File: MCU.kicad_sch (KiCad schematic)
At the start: 36 parts

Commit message: Updates to schematic
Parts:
- removed C?: 100n, Capacitor_SMD:C_0603_1608Metric_Pad1.08x0.95mm_HandSolder, symbol Device:C_Small
- removed D? (x4): BAT54S, Package_TO_SOT_SMD:SOT-23, symbol Diode:BAT54S
- removed J?: LED_MCU_ON, symbol Connector_Generic:Conn_01x02
- removed J?: DNP, Connector_Coaxial:U.FL_Molex_MCRF_73412-0110_Vertical, symbol Connector:Conn_Coaxial
- removed R?: 470, Resistor_SMD:R_0603_1608Metric_Pad0.98x0.95mm_HandSolder, symbol Device:R
- removed R? (x2): 10k, Resistor_SMD:R_0603_1608Metric_Pad0.98x0.95mm_HandSolder, symbol Device:R
- removed U?: 74LVC1G66, Package_TO_SOT_SMD:SOT-353_SC-70-5_Handsoldering, symbol 74xGxx:74LVC1G66
- added C? (x5): 100n, Capacitor_SMD:C_0603_1608Metric_Pad1.08x0.95mm_HandSolder, symbol Device:C_Small
- added D?: PLL_LOCK, LED_SMD:LED_0603_1608Metric_Pad1.05x0.95mm_HandSolder, symbol Device:LED
- added D? (x8): (no value), LED_SMD:LED_0603_1608Metric_Pad1.05x0.95mm_HandSolder, symbol Device:LED
- added D? (x12): PESD3V3L4UG, Package_TO_SOT_SMD:SOT-353_SC-70-5, symbol Power_Protection:PESD3V3L4UG
- added FB?: TODO, symbol Device:FerriteBead_Small
- added J? (x2): Conn_01x03, symbol Connector_Generic:Conn_01x03
- added J?: Conn_01x06, symbol Connector_Generic:Conn_01x06
- added R? (x4): 100, Resistor_SMD:R_0603_1608Metric_Pad0.98x0.95mm_HandSolder, symbol Device:R
- added R? (x9): 2k, Resistor_SMD:R_0603_1608Metric_Pad0.98x0.95mm_HandSolder, symbol Device:R
- added R? (x5): 10k, Resistor_SMD:R_0603_1608Metric_Pad0.98x0.95mm_HandSolder, symbol Device:R
- added R?: 3k3, Resistor_SMD:R_0603_1608Metric_Pad0.98x0.95mm_HandSolder, symbol Device:R
- added R?: NC, Resistor_SMD:R_0603_1608Metric_Pad0.98x0.95mm_HandSolder, symbol Device:R
- added U? (x2): 74HC4094, Package_SO:SO-16_3.9x9.9mm_P1.27mm, symbol petr:74HC4094
- added U?: SN75176AD, Package_SO:SOIC-8_3.9x4.9mm_P1.27mm, symbol Interface_UART:SN75176AD
- added Y?: Crystal_GND24, symbol Device:Crystal_GND24
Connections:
- net AVDD: now also FB?.2
- net CE: now also U?.12 (Q6)
- net CLK_SEL: now also R?.2, U?.7 (Q3)
- net CSB: now also U?.28 (PA07)
- net DIVA: now also U?.40 (PD00)
- net DIVB: now also U?.39 (PD01)
- net GND: now also C?.2, C?.2, C?.2, C?.2, C?.2, D?.2 (A), D?.2 (A), D?.2 (A), J?.3 (Pin_3), J?.3 (Pin_3), J?.6 (Pin_6), R?.1, R?.1, R?.1, R?.1, R?.2, R?.2, R?.2, R?.2, R?.2, R?.2, R?.2, R?.2, R?.2, R?.2, U?.5 (GND), U?.8 (GND), U?.8 (GND), Y?.2, Y?.4
- net LOS_0: now also U?.17 (PB03)
- net LOS_1: now also U?.16 (PB04)
- net MUXout: now also U?.27 (PA06)
- net OE_B: now also R?.2, U?.13 (Q5)
- net PLL_ON: now also U?.4 (Q0)
- net RampClk: now also U?.29 (PA08)
- net RampDir: now also U?.11 (Q7)
- net SCK: now also U?.25 (PA04)
- net SDI: now also U?.26 (PA05)
- net SFOUTB_0: now also U?.38 (PD02)
- net SFOUTB_1: now also U?.37 (PD03)
- net SWCLK: now also D?.5 (K4)
- net SWDIO: now also D?.4 (K3)
- net SWO: now also D?.3 (K2)
- net TCXO_ON: now also U?.6 (Q2)
- net VCC_TCXO: now also U?.21 (PA00)
- net fREF_ON: now also U?.5 (Q1)
- net ~{DF_CORR_EN}: now also U?.14 (Q4)
- net AUX_CLK: now reaches U?.1 (PC00)
- net AUX_CLK: now also R?.1, U?.3 (CP), U?.3 (CP)
- net at U?.10 (HFXTAL_O): now also Y?.3
- net ~{RESET}: now reaches U?.11 (RESETN)
- net ~{RESET}: now also C?.1, D?.1 (K1), R?.1
- net RS485_DIR: now reaches U?.18 (PB02)
- net RS485_DIR: now also R?.1, U?.2 (~{RE}), U?.3 (DE)
- net RS485_TX: now reaches U?.19 (PB01)
- net RS485_TX: now also U?.4 (D)
- net AUX_D: now reaches U?.2 (PC01)
- net AUX_D: now also U?.2 (D)
- net RS485_RX: now reaches U?.20 (PB00)
- net RS485_RX: now also U?.1 (R)
- net AUX_STR: now reaches U?.3 (PC02)
- net AUX_STR: now also R?.1, U?.1 (STR), U?.1 (STR)
- net AUX_OE: now reaches U?.4 (PC03)
- net AUX_OE: now also D?.5 (K4), J?.5 (Pin_5), R?.2, U?.15 (OE), U?.15 (OE)
- net DUTY: now reaches U?.5 (PC04)
- net VCC_PLL: now reaches U?.6 (PC05)
- net VCC_fREF: now reaches U?.7 (PC06)
- net at U?.8 (PC07): now also D?.2 (A)
- net at U?.9 (HFXTAL_I): now also Y?.1
- net at J?.10 (~{RESET}): now also R?.2
- net VCC renamed VCC_MCU
- net VCC_MCU: now also C?.1, C?.1, C?.1, C?.1, D?.5 (K4), FB?.1, J?.1 (Pin_1), R?.1, R?.1, U?.16 (VCC), U?.16 (VCC), U?.8 (VCC)
- new net: D?.1 (K1), J?.2 (Pin_2), R?.2
- new net: D?.1 (K), R?.1 (x9)
- new net: R?.1, U?.10 (QS2)
- new net: D?.2 (A), U?.11 (Q7)
- new net: D?.2 (A), U?.12 (Q6)
- new net: D?.2 (A), U?.13 (Q5)
- new net: D?.2 (A), U?.14 (Q4)
- new net: U?.10 (QS2), U?.2 (D)
- new net: D?.2 (A), U?.4 (Q0)
- new net: D?.2 (A), U?.5 (Q1)
- new net: D?.2 (A), U?.6 (Q2)
- new net: D?.2 (A), U?.7 (Q3)
- new net: D?.3 (K2), J?.1 (Pin_1), J?.1 (Pin_1), R?.2, U?.6 (A)
- new net: D?.4 (K3), J?.4 (Pin_4), R?.2
- new net: D?.1 (K1), J?.2 (Pin_2), J?.2 (Pin_2), R?.2, U?.7 (B)
- new net: D?.3 (K2), J?.3 (Pin_3), R?.2
- no-connect marks 2 -> 4
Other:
- note added: "Analog reference voltage"
- note added: "Auxiliary circuitry"
- note added: "Auxiliary control signals"
- note added: "Auxiliary indicators"
- note added: "Debug interface"
- note added: "Do not change this value, matches internal pullup."
- note added: "Expansion port"
- note added: "If no device next in chain is connected, connect termination resistor to the unused port."
- note added: "Microcontroller"
- note added: "PLL"
- note added: "POWER"
- note added: "RS485"
- note added: "RS485 interface"
- note added: "SWD"
- note added: "fREF"
- note removed: "Debug"
- note removed: "The AVDD voltage should be under 3.0 V, when the TCXO reference starts, it should jump to 3.3V automatically."
- moved on the sheet: C?, D?, J?, L?, R?, U?, U?A, U?B

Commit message: Finished schematics
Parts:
- added R425: 0R, Resistor_SMD:R_0603_1608Metric_Pad0.98x0.95mm_HandSolder, symbol Device:R
- gave numbers to parts that had none: 69
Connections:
- net DVDD: now also R419.2
- net GND: now also R425.2; no longer C416.2
- new net: C416.2, R425.1
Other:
- company: (none) -> Petr Polasek
- title: (none) -> Generator 0.0125 - 6.4 GHz (0.02 - 9.8 GHz)
- moved on the sheet: C402, C403, C404, D401, D402, D403, D404, D405, D406, D407, D408, R406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

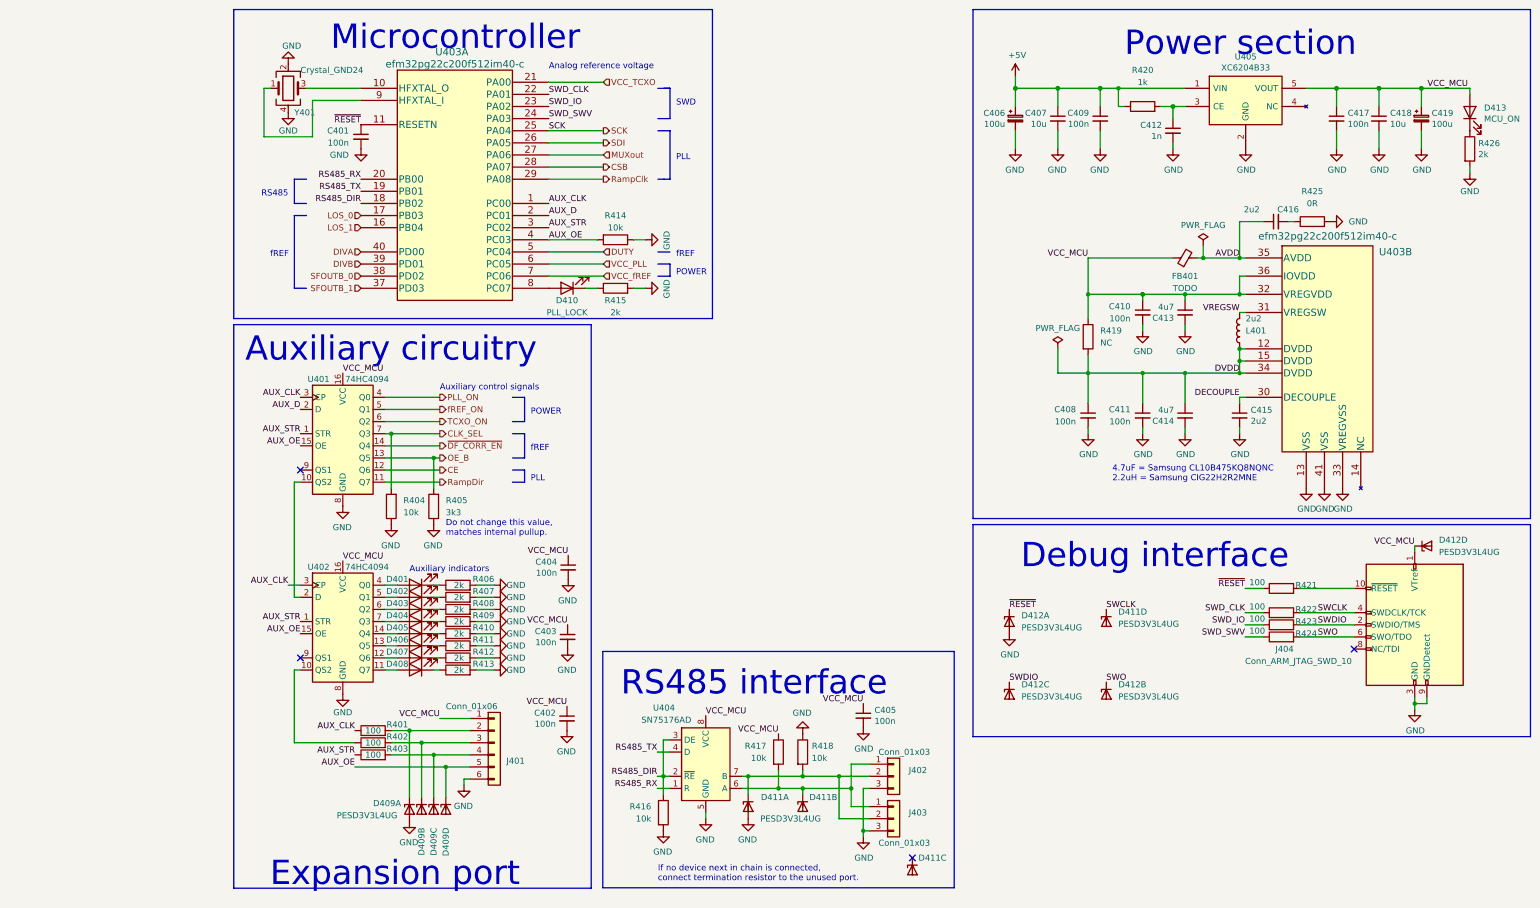
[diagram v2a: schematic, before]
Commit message: Schematic fixes
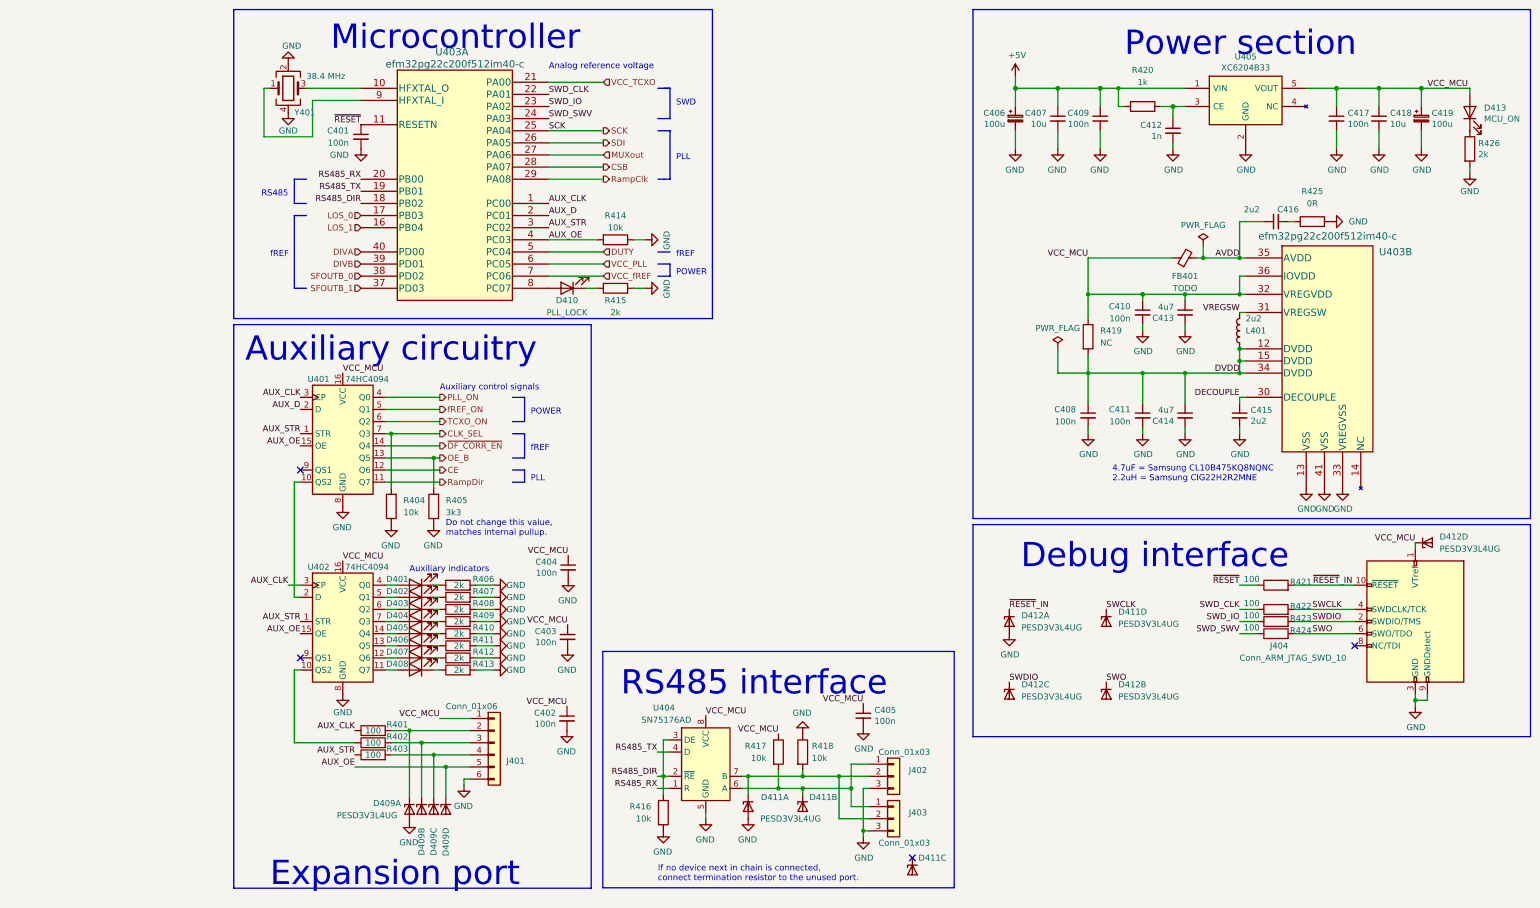
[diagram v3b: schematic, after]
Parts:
- Y401: value Crystal_GND24 -> 38.4 MHz
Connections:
- net ~{RESET}: no longer D412.1 (K1)
- net ~{RESET}_IN: now reaches J404.10 (~{RESET}), R421.2
- net ~{RESET}_IN: now also D412.1 (K1)
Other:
- moved on the sheet: D412D, J404, R421, R422, R423, R424

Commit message: Schematic checked. All footprints assigned. Electrolytics need footprint check, so do the RS485 and power connectors and the MuRata oscillator (also it is now EOL) and the crystal. The power protection transils on aux input/output need replacement. PCB in sync with SCH.
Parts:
- removed D410: PLL_LOCK, LED_SMD:LED_0603_1608Metric_Pad1.05x0.95mm_HandSolder, symbol Device:LED
- removed J401: Conn_01x06, symbol Connector_Generic:Conn_01x06
- added J401: Conn_01x07, Connector_PinHeader_2.54mm:PinHeader_1x07_P2.54mm_Vertical, symbol Connector_Generic:Conn_01x07
- added R427: 100, Resistor_SMD:R_0603_1608Metric_Pad0.98x0.95mm_HandSolder, symbol Device:R
- added R428: 10k, Resistor_SMD:R_0603_1608Metric_Pad0.98x0.95mm_HandSolder, symbol Device:R
- FB401: footprint (none) -> Inductor_SMD:L_0603_1608Metric_Pad1.05x0.95mm_HandSolder
- J402, J403: footprint (none) -> Connector_Phoenix_MSTB:PhoenixContact_MSTBA_2,5_3-G-5,08_1x03_P5.08mm_Horizontal
- L401: footprint (none) -> Inductor_SMD:L_1008_2520Metric_Pad1.43x2.20mm_HandSolder
- R415: value 2k -> 100
- Y401: footprint (none) -> Crystal:Crystal_SMD_2016-4Pin_2.0x1.6mm
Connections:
- net AUX_OE: now also R415.1; no longer D409.5 (K4)
- net DUTY: now also U403.6 (PC05); no longer U403.5 (PC04)
- net GND: now also J401.7 (Pin_7), R428.1; no longer R415.2
- net SWCLK: now also D412.5 (K4); no longer D411.5 (K4)
- net VCC_MCU: now also D411.5 (K4), J401.1 (Pin_1); no longer D412.5 (K4)
- net VCC_PLL: now also U403.7 (PC06); no longer U403.6 (PC05)
- net VCC_fREF: now also U403.8 (PC07); no longer U403.7 (PC06)
- net at D409.1 (K1), R401.2: now also J401.2 (Pin_2)
- net at D409.4 (K3), R403.2: now also J401.4 (Pin_4)
- net at D409.3 (K2), R402.2: now also J401.3 (Pin_3)
- net at D411.4 (K3): now also J401.6 (Pin_6), R427.2
- new net: D409.5 (K4), J401.5 (Pin_5), R415.2
- new net AUX_MISO: R427.1, R428.2, U403.5 (PC04)
- no-connect marks 4 -> 3
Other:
- moved on the sheet: D409A, D409B, D409C, D409D, D411C, D411D, D412D, R401, R402, R403

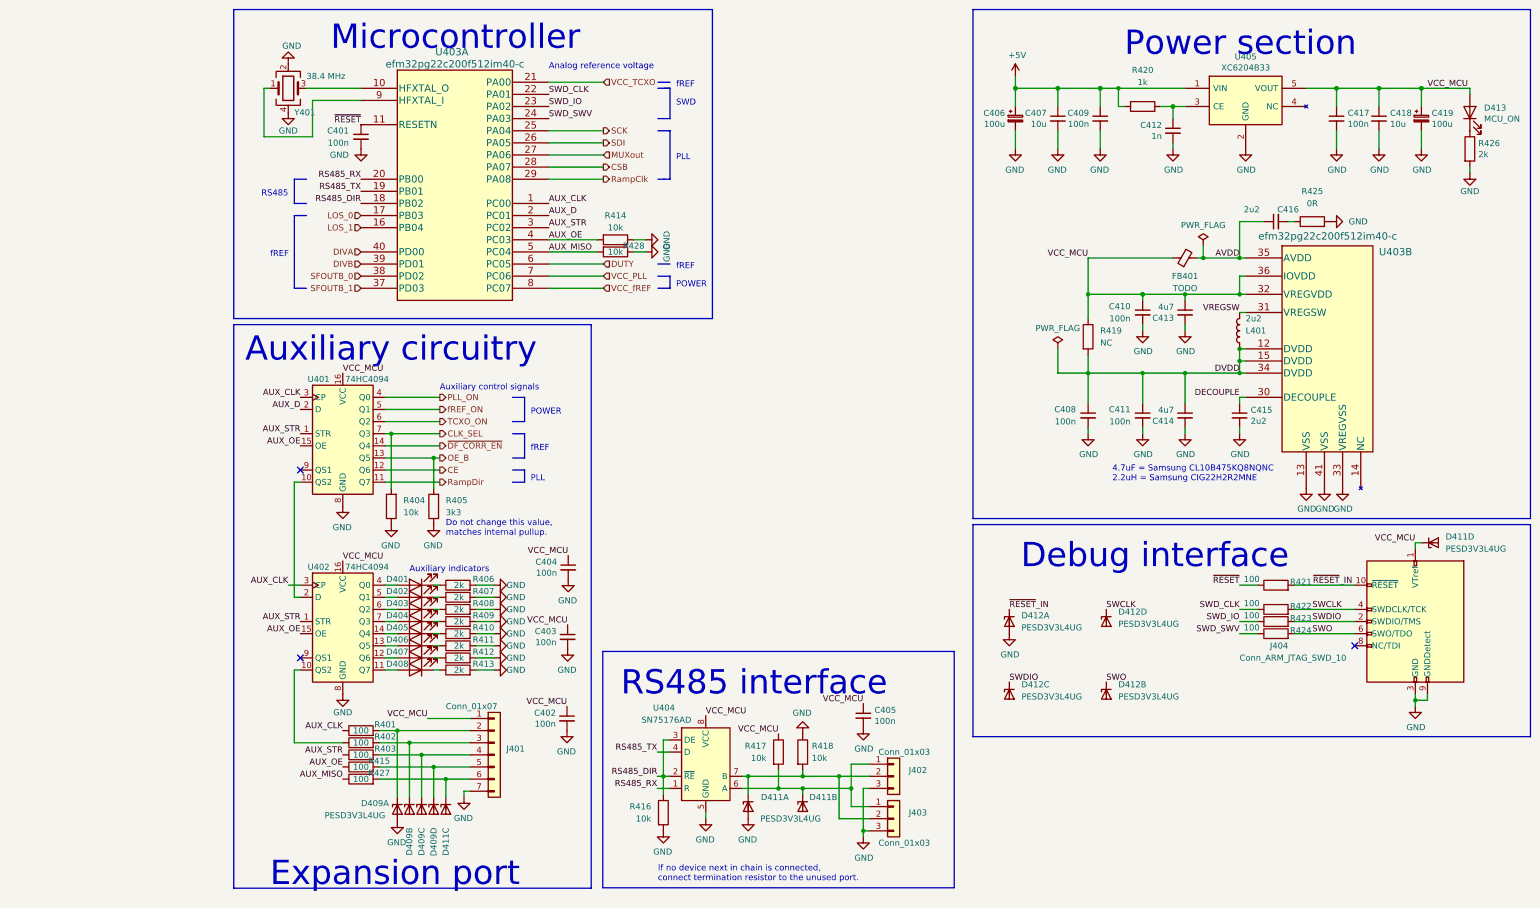
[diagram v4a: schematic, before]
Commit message: Resolved all broken symbols / packages / links except TCXO.
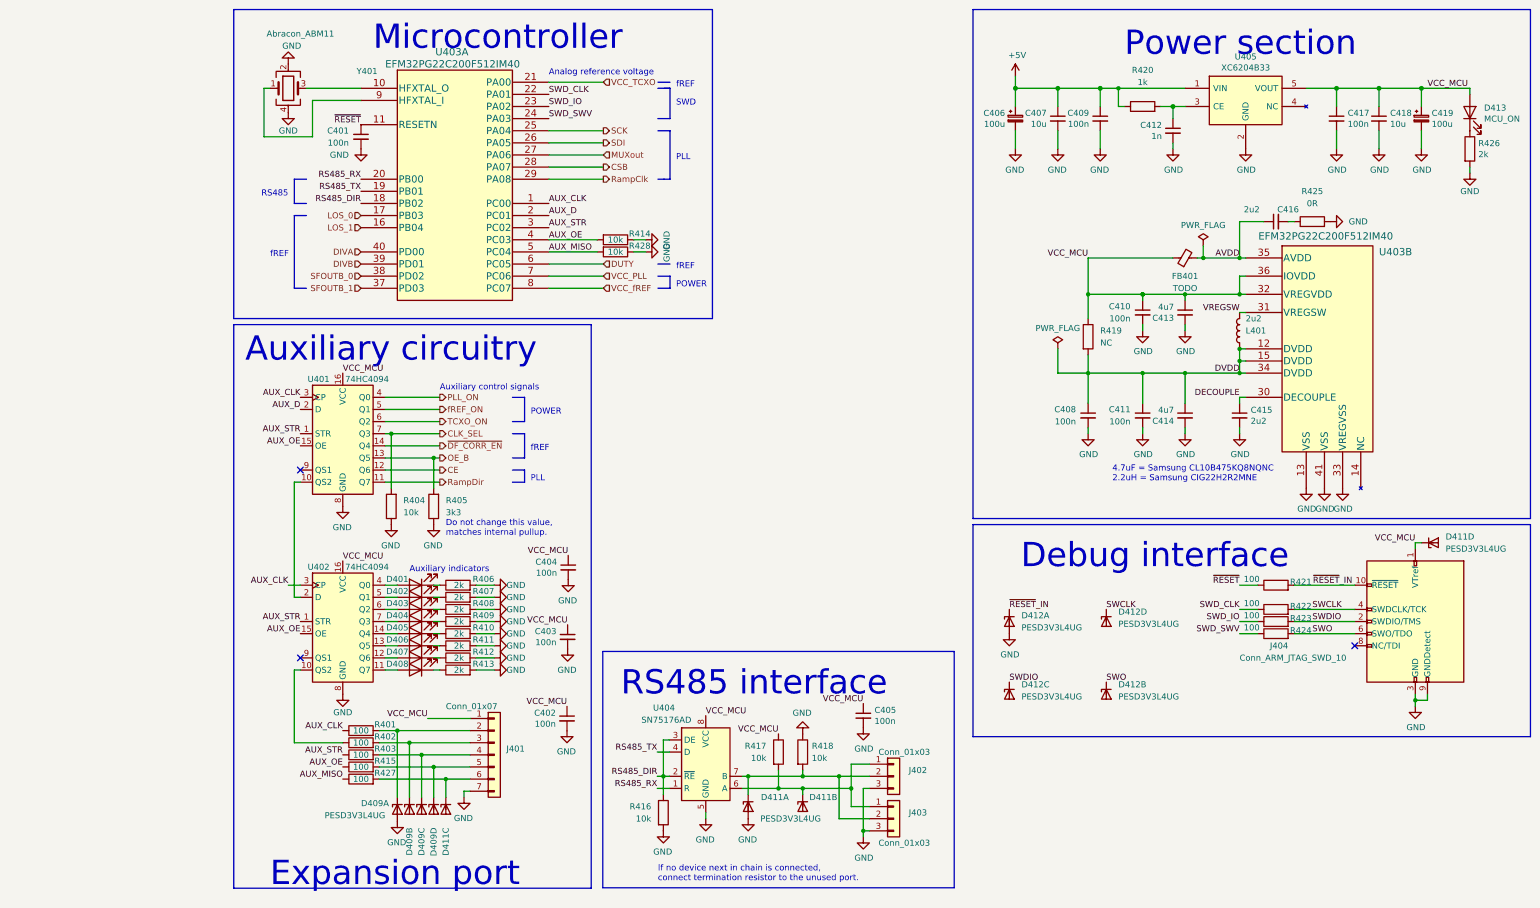
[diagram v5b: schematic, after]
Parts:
- removed Y401: 38.4 MHz, Crystal:Crystal_SMD_2016-4Pin_2.0x1.6mm, symbol Device:Crystal_GND24
- added Y401: Abracon_ABM11, petr:Crystal_SMD_Abracon_ABM3-4Pin_2.0x1.6mm, symbol petr:Abracon_ABM11
- U403: value efm32pg22c200f512im40-c -> EFM32PG22C200F512IM40; footprint EFM32PG22C200:efm32pg22c200f512im40-c -> petr:EFM32PG22C200F512IM40; symbol EFM32PG22C200:efm32pg22c200f512im40-c -> petr:EFM32PG22C200F512IM40
- U405: symbol petr_lib_nightly:XC6204B33 -> petr:XC6204B33
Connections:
- net GND: now also Y401.2, Y401.4
- net at U403.10 (HFXTAL_O): now also Y401.3
- net at U403.9 (HFXTAL_I): now also Y401.1

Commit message: Footprint changes
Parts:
- C406, C419: footprint Capacitor_SMD:CP_Elec_6.3x7.7 -> Capacitor_SMD:CP_Elec_6.3x5.8; symbol Device:C_Polarized_Small -> petr:CP_47uF_35V
- J401: value Conn_01x07 -> EXPANSION_PORT
- J402: value Conn_01x03 -> RS485_1
- J403: value Conn_01x03 -> RS485_2
- J404: symbol Connector:Conn_ARM_JTAG_SWD_10 -> petr:Conn_ARM_JTAG_SWD_9
- U404: symbol Interface_UART:SN75176AD -> petr:SN75HVD11D
